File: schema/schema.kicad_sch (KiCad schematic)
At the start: 13 parts, among them J1 Conn_01x15, J2 Conn_01x15, J3 Conn_01x15, J4 Conn_01x15, J5 Conn_01x03, SW1 SW_Push, SW2 SW_Push, SW3 SW_Push

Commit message: Finish transmitter-board schema
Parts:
- D1: value LED -> LED_TX
- D2: value LED -> LED_STATUS
- J1, J2, J3, J4: value Conn_01x15 -> MCU_ATmega328P_Module
- J5: value Conn_01x03 -> RF_433MHz_TX
- SW1: value SW_Push -> BTN_MORSE
- SW2: value SW_Push -> BTN_SPEED_UP
- SW3: value SW_Push -> BTN_SPEED_DOWN
- renumbered R1 to R220Ω, R2 to R220Ω
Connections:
- net at D1.1 (K): now also R220Ω.2
- net GND: now reaches D1.2 (A)
- net GND: now also BZ1.2 (-), D2.2 (A), J1.2 (Pin_2), J4.2 (Pin_2), J5.3 (Pin_3), SW1.2, SW2.2, SW3.2
- net at SW2.1: now also J2.8 (Pin_8)
- net at D2.1 (K): now also R220Ω.2
- net at J2.10 (Pin_10): now also R220Ω.1
- net DATA: now reaches J2.13 (Pin_13)
- net DATA: now also J5.2 (Pin_2)
- net at J2.5 (Pin_5): now also BZ1.1 (+)
- net at J2.6 (Pin_6): now also SW3.1
- net at J2.7 (Pin_7): now also SW1.1
- net at J2.9 (Pin_9): now also R220Ω.1
- net 5V: now reaches J5.1 (Pin_1)
- net 5V: now also J1.4 (Pin_4), J4.4 (Pin_4)
- net VIN: now reaches J4.1 (Pin_1)
- net VIN: now also J1.1 (Pin_1)
- net A2: now reaches J4.10 (Pin_10)
- net A2: now also J1.10 (Pin_10)
- net A1: now reaches J4.11 (Pin_11)
- net A1: now also J1.11 (Pin_11)
- net A0: now reaches J4.12 (Pin_12)
- net A0: now also J1.12 (Pin_12)
- net REF: now reaches J4.13 (Pin_13)
- net REF: now also J1.13 (Pin_13)
- net 3V3: now reaches J4.14 (Pin_14)
- net 3V3: now also J1.14 (Pin_14)
- net D13: now reaches J4.15 (Pin_15)
- net D13: now also J1.15 (Pin_15)
- net RST: now reaches J4.3 (Pin_3)
- net RST: now also J1.3 (Pin_3)
- net A7: now reaches J4.5 (Pin_5)
- net A7: now also J1.5 (Pin_5)
- net A6: now reaches J4.6 (Pin_6)
- net A6: now also J1.6 (Pin_6)
- net A5: now reaches J4.7 (Pin_7)
- net A5: now also J1.7 (Pin_7)
- net A4: now reaches J4.8 (Pin_8)
- net A4: now also J1.8 (Pin_8)
- net A3: now reaches J4.9 (Pin_9)
- net A3: now also J1.9 (Pin_9)
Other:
- note added: "5V"
- note added: "D10"
- note added: "D2"
- note added: "D3"
- note added: "D4"
- note added: "D5"
- note added: "D6"
- note added: "D7"
- note added: "GND"
- moved on the sheet: D1, D2, R220Ω, SW1, SW2, SW3

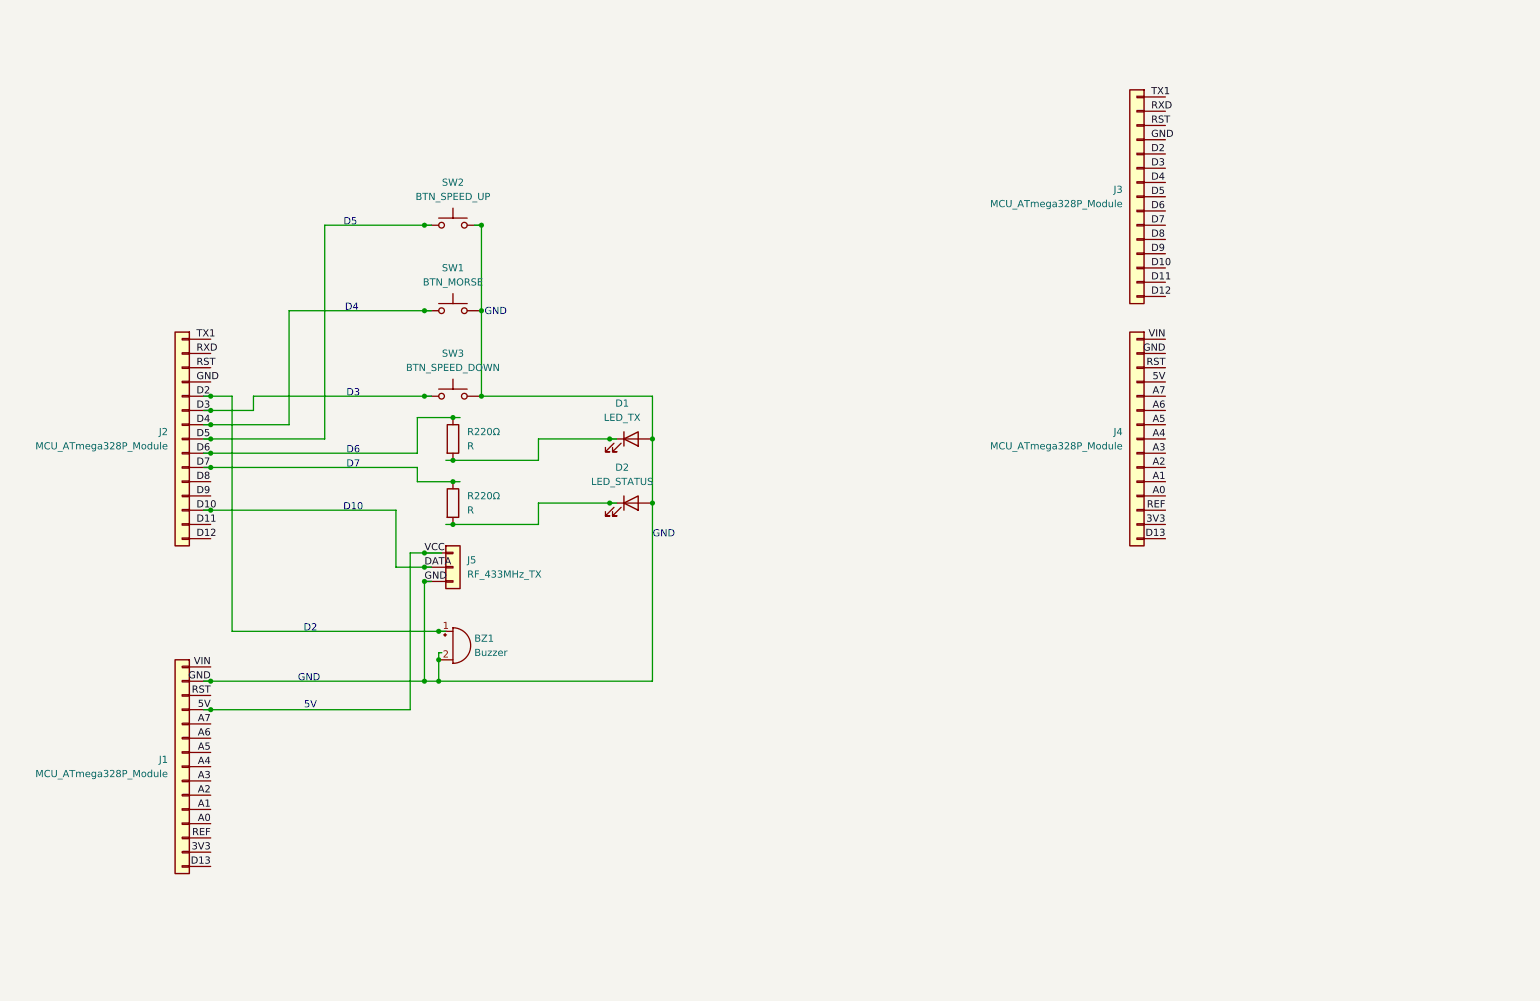
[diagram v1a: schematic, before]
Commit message: Prepare schema for checkpoint
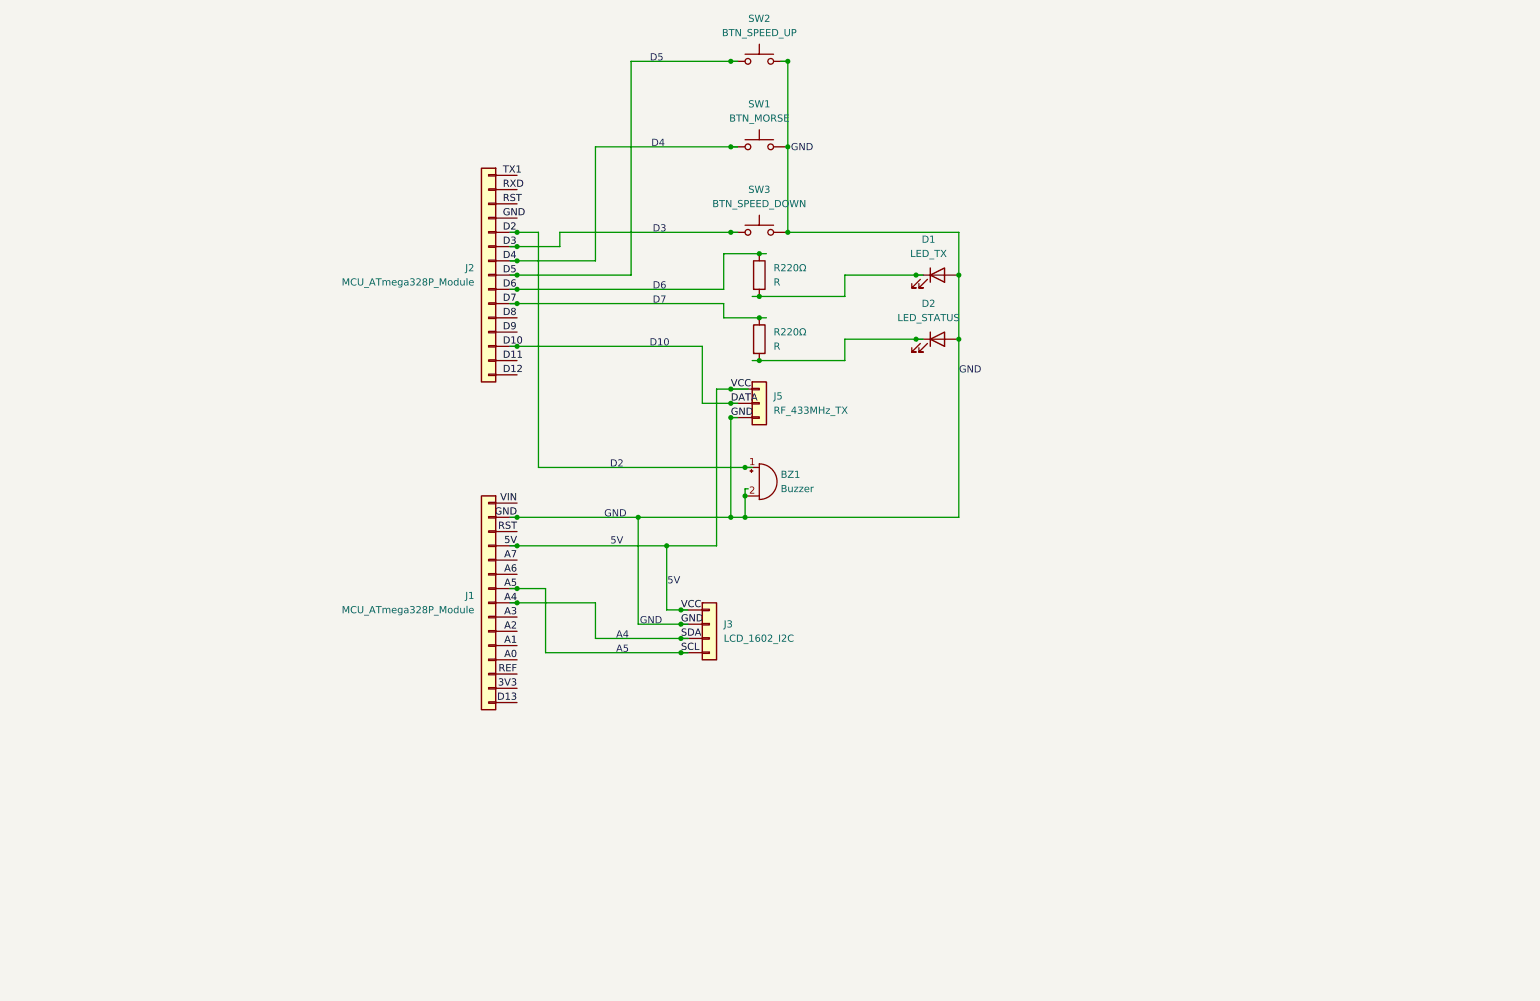
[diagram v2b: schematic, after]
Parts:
- removed J3, J4: MCU_ATmega328P_Module, symbol Connector_Generic:Conn_01x15
- added J3: LCD_1602_I2C, symbol Connector_Generic:Conn_01x04
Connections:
- net 5V: now also J3.1 (Pin_1)
- net A4: now also J3.3 (Pin_3)
- net A5: now also J3.4 (Pin_4)
- net GND: now also J3.2 (Pin_2)
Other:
- note added: "A4"
- note added: "A5"
- moved on the sheet: BZ1, D1, D2, J1, J2, J5, R220Ω, SW1, SW2, SW3

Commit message: Prepare schema for final project
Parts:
- added J4, J6: MCU_ATmega328P_Module, symbol Connector_Generic:Conn_01x15
- added J7: RF_433MHz_RX, symbol Connector_Generic:Conn_01x04
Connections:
- net 3V3: now also J6.14 (Pin_14)
- net 5V: now also J6.4 (Pin_4), J7.4 (Pin_4)
- net A0: now also J6.12 (Pin_12)
- net A1: now also J6.11 (Pin_11)
- net A2: now also J6.10 (Pin_10)
- net A3: now also J6.9 (Pin_9)
- net A4: now also J6.8 (Pin_8)
- net A5: now also J6.7 (Pin_7)
- net A6: now also J6.6 (Pin_6)
- net A7: now also J6.5 (Pin_5)
- net D13: now also J6.15 (Pin_15)
- net D2: now also J4.5 (Pin_5), J7.2 (Pin_2)
- net GND: now also J6.2 (Pin_2), J7.1 (Pin_1)
- net REF: now also J6.13 (Pin_13)
- net RST: now also J6.3 (Pin_3)
- net VIN: now also J6.1 (Pin_1)
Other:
- moved on the sheet: BZ1, D1, D2, J1, J2, J3, J5, R220Ω, SW1, SW2, SW3

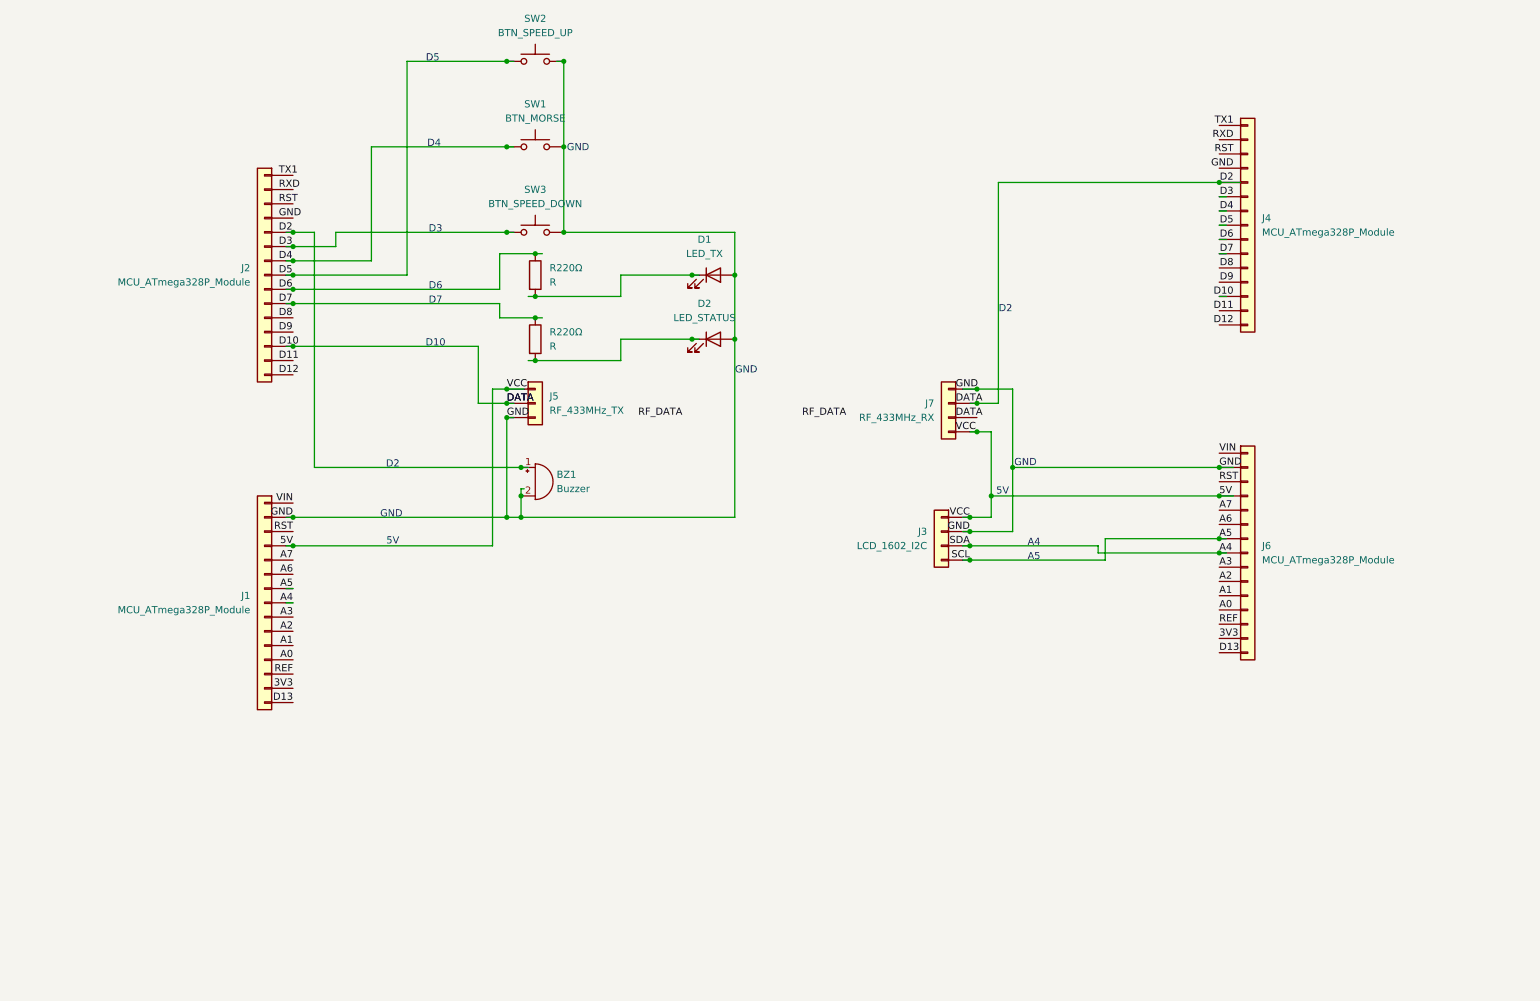
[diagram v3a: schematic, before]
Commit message: Add description to schema
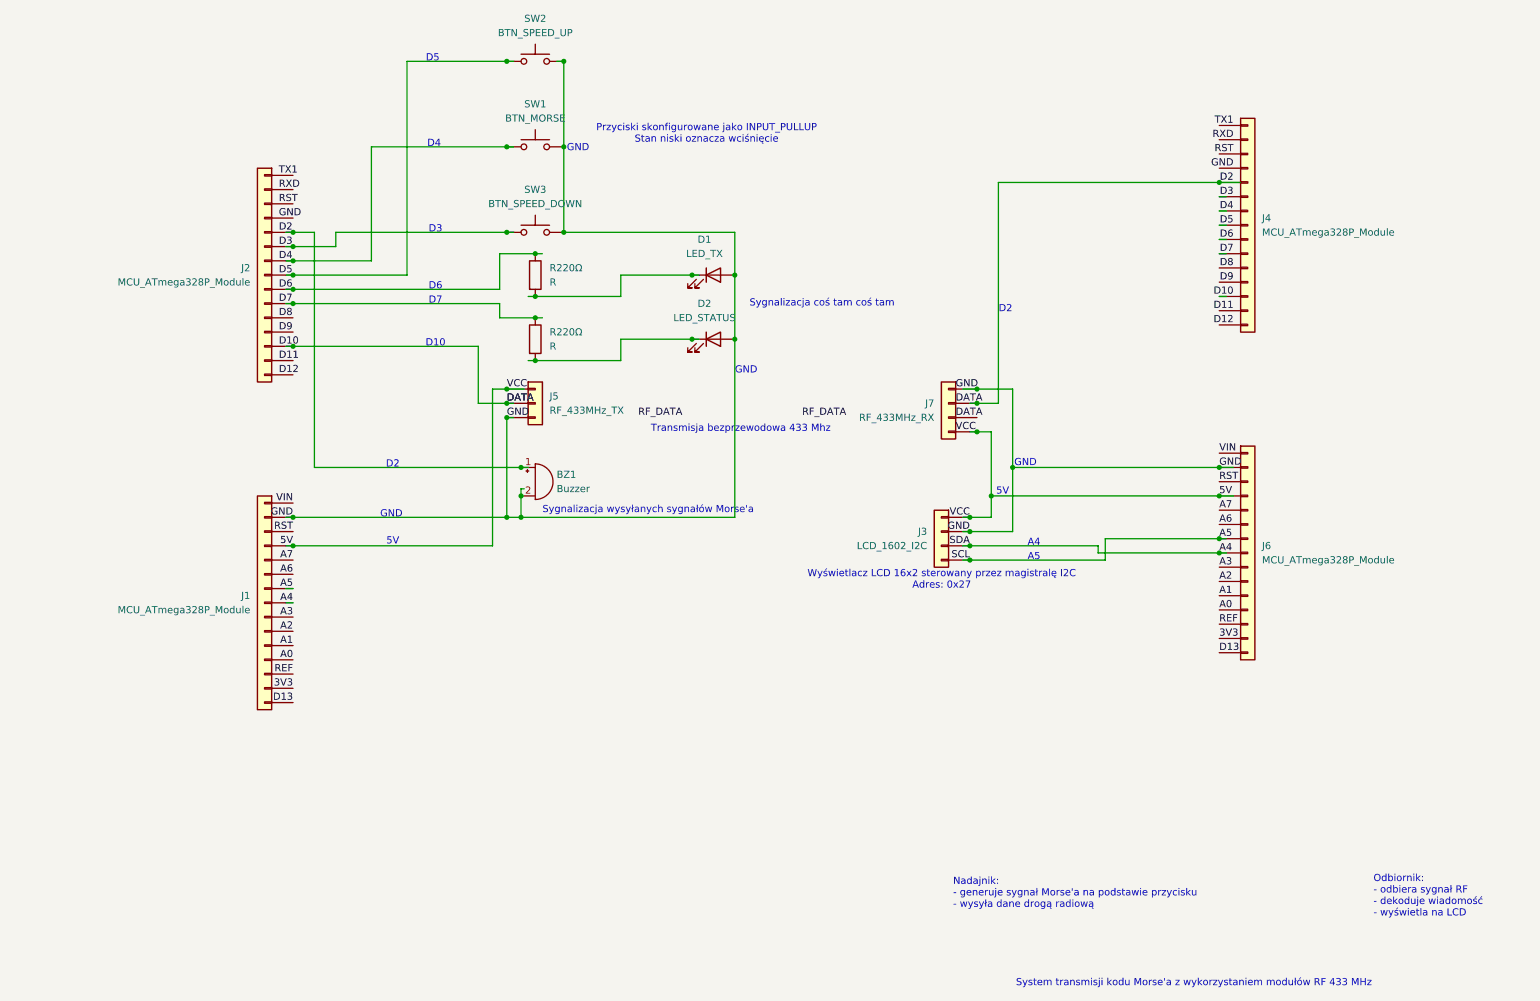
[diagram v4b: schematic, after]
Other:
- note added: "Nadajnik: - generuje sygnał Morse'a na podstawie przycisku - wysyła dane drogą radiową"
- note added: "Odbiornik: - odbiera sygnał RF - dekoduje wiadomość - wyświetla na LCD"
- note added: "Przyciski skonfigurowane jako INPUT_PULLUP Stan niski oznacza wciśnięcie"
- note added: "Sygnalizacja coś tam coś tam"
- note added: "Sygnalizacja wysyłanych sygnałów Morse'a"
- note added: "System transmisji kodu Morse'a z wykorzystaniem modułów RF 433 MHz"
- note added: "Transmisja bezprzewodowa 433 Mhz"
- note added: "Wyświetlacz LCD 16x2 sterowany przez magistralę I2C Adres: 0x27"
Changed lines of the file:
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@@
+		)
+	)
+	(text "System transmisji kodu Morse'a z wykorzystaniem modułów RF 433 MHz"
+		(exclude_from_sim no)
+		(at 222.25 189.738 0)
+		(effects
+			(font
+				(size 1.27 1.27)
+			)
 		)
 	)
@@
 		)
 	)
+	(text "Przyciski skonfigurowane jako INPUT_PULLUP\nStan niski oznacza wciśnięcie"
+		(exclude_from_sim no)
+		(at 135.382 38.354 0)
+		(effects
+			(font
+				(size 1.27 1.27)
+			)
+		)
+	)
 	(text "A4"
 		(exclude_from_sim no)
 		(at 193.7456 111.252 0)
+		(effects
+			(font
+				(size 1.27 1.27)
+			)
+		)
+	)
+	(text "Wyświetlacz LCD 16x2 sterowany przez magistralę I2C\nAdres: 0x27"
+		(exclude_from_sim no)
+		(at 177.292 117.856 0)
 		(effects
 			(font
@@
 		(effects
 			(font
+				(size 1.27 1.27)
+			)
+		)
+	)
+	(text "Nadajnik:\n- generuje sygnał Morse'a na podstawie przycisku\n- wysyła dane drogą radiową"
+		(exclude_from_sim no)
+		(at 179.324 173.736 0)
+		(effects
+			(font
+				(size 1.27 1.27)
+			)
+			(justify left)
+		)
+	)
+	(text "Odbiornik:\n- odbiera sygnał RF\n- dekoduje wiadomość\n- wyświetla na LCD"
+		(exclude_from_sim no)
+		(at 254.254 174.244 0)
+		(effects
+			(font
+				(size 1.27 1.27)
+			)
+			(justify left)
+		)
+	)
+	(text "Sygnalizacja wysyłanych sygnałów Morse'a"
+		(exclude_from_sim no)
+		(at 124.968 105.41 0)
+		(effects
+			(font
+				(size 1.27 1.27)
+			)
+		)
+	)
+	(text "Transmisja bezprzewodowa 433 Mhz"
+		(exclude_from_sim no)
+		(at 141.478 90.932 0)
+		(effects
+			(font
+				(size 1.27 1.27)
+			)
+		)
+	)
+	(text "Sygnalizacja coś tam coś tam"
+		(exclude_from_sim no)
+		(at 155.956 68.58 0)
+		(effects
+			(font
